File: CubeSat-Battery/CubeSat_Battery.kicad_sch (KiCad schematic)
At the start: 3 parts, among them J1 Conn_01x02_Pin, J2 Conn_01x02_Pin, U1 BatteryPack

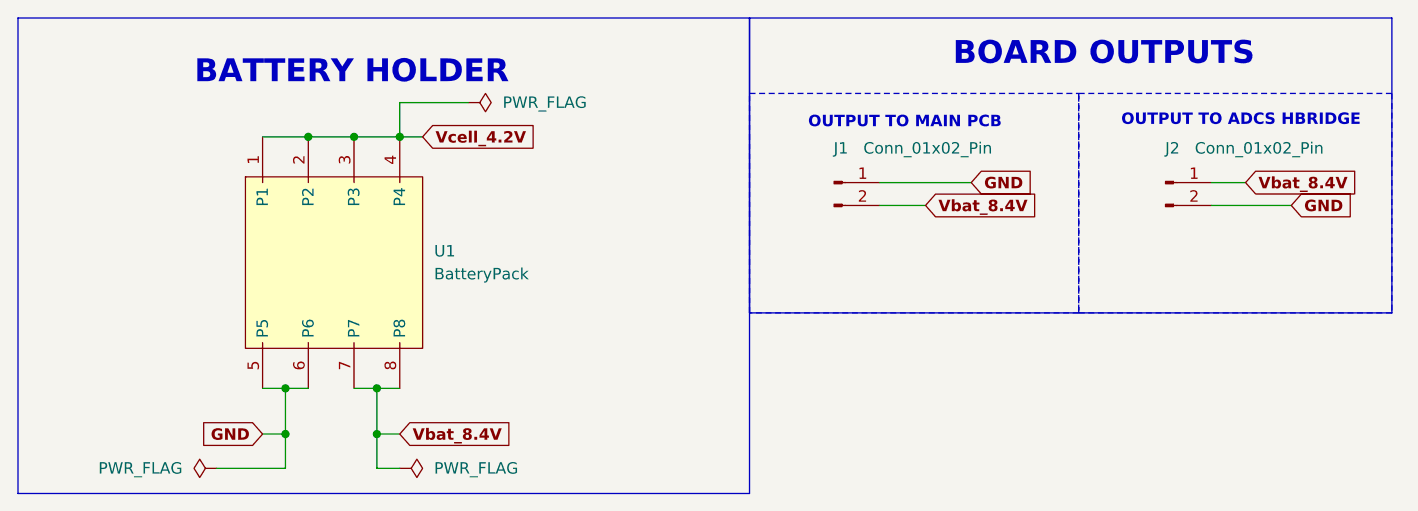
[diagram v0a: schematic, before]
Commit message: final version of the 3 PCBs, minor size changes for the protoypes
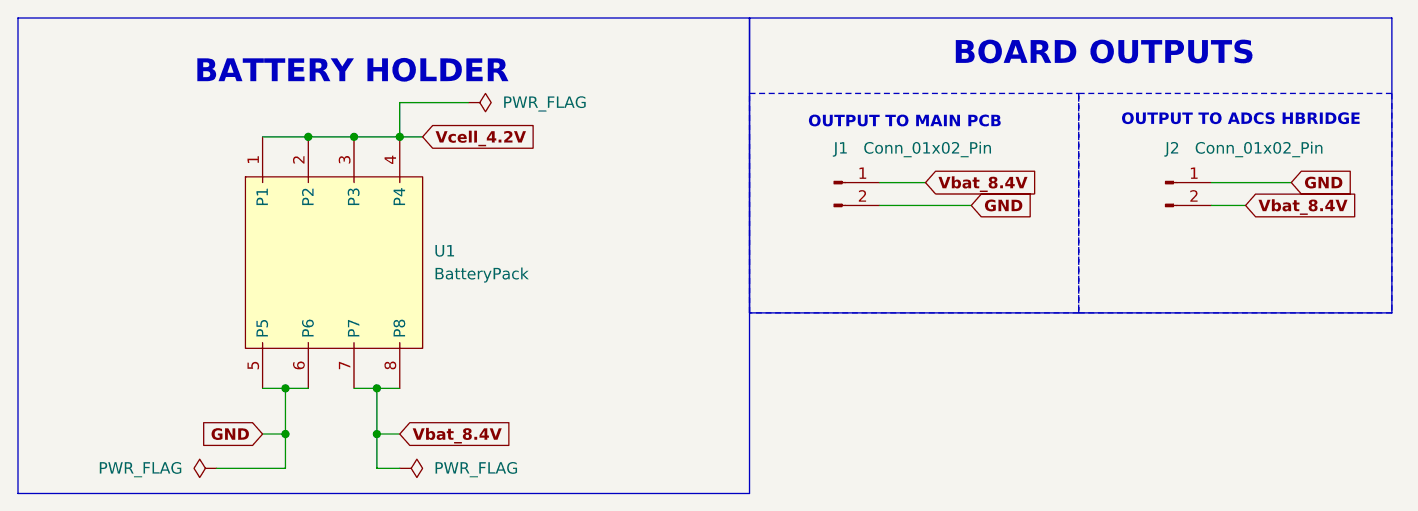
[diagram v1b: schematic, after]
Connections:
- net GND: now also J1.2 (Pin_2), J2.1 (Pin_1); no longer J1.1 (Pin_1), J2.2 (Pin_2)
- net Vbat_8.4V: now also J1.1 (Pin_1), J2.2 (Pin_2); no longer J1.2 (Pin_2), J2.1 (Pin_1)
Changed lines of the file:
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@@
-	(wire
-		(pts
-			(xy 107.95 33.02) (xy 113.03 33.02)
-		)
-		(stroke
-			(width 0)
-			(type default)
-		)
-	)
 	(wire
 		(pts
@@
 	(wire
 		(pts
+			(xy 107.95 30.48) (xy 113.03 30.48)
+		)
+		(stroke
+			(width 0)
+			(type default)
+		)
+	)
+	(wire
+		(pts
 			(xy 41.91 53.34) (xy 44.45 53.34)
 		)
@@
 	(wire
 		(pts
-			(xy 107.95 30.48) (xy 118.11 30.48)
+			(xy 144.78 33.02) (xy 148.59 33.02)
 		)
 		(stroke
@@
 	(wire
 		(pts
-			(xy 144.78 30.48) (xy 148.59 30.48)
-		)
-		(stroke
-			(width 0)
-			(type default)
-		)
-	)
-	(wire
-		(pts
 			(xy 49.53 53.34) (xy 52.07 53.34)
 		)
@@
 	(wire
 		(pts
+			(xy 144.78 30.48) (xy 153.67 30.48)
+		)
+		(stroke
+			(width 0)
+			(type default)
+		)
+	)
+	(wire
+		(pts
 			(xy 52.07 58.42) (xy 52.07 62.23)
 		)
@@
 	(wire
 		(pts
-			(xy 144.78 33.02) (xy 153.67 33.02)
-		)
-		(stroke
-			(width 0)
-			(type default)
-		)
-	)
-	(wire
-		(pts
 			(xy 54.61 25.4) (xy 57.15 25.4)
 		)
@@
 		)
 	)
+	(wire
+		(pts
+			(xy 107.95 33.02) (xy 118.11 33.02)
+		)
+		(stroke
+			(width 0)
+			(type default)
+		)
+	)
 	(global_label "GND"
 		(shape input)
@@
 	(global_label "GND"
 		(shape input)
-		(at 153.67 33.02 0)
-		(fields_autoplaced yes)
-		(effects
-			(font
-				(size 1.27 1.27)
-				(thickness 0.254)
-				(bold yes)
-			)
-			(justify left)
-		)
-		(property "Intersheetrefs" "${INTERSHEET_REFS}"
-			(at 161.0017 33.02 0)
+		(at 153.67 30.48 0)
+		(fields_autoplaced yes)
+		(effects
+			(font
+				(size 1.27 1.27)
+				(thickness 0.254)
+				(bold yes)
+			)
+			(justify left)
+		)
+		(property "Intersheetrefs" "${INTERSHEET_REFS}"
+			(at 161.0017 30.48 0)
 			(effects
 				(font
@@
 	(global_label "GND"
 		(shape input)
-		(at 118.11 30.48 0)
-		(fields_autoplaced yes)
-		(effects
-			(font
-				(size 1.27 1.27)
-				(thickness 0.254)
-				(bold yes)
-			)
-			(justify left)
-		)
-		(property "Intersheetrefs" "${INTERSHEET_REFS}"
-			(at 125.4417 30.48 0)
+		(at 118.11 33.02 0)
+		(fields_autoplaced yes)
+		(effects
+			(font
+				(size 1.27 1.27)
+				(thickness 0.254)
+				(bold yes)
+			)
+			(justify left)
+		)
+		(property "Intersheetrefs" "${INTERSHEET_REFS}"
+			(at 125.4417 33.02 0)
 			(effects
 				(font
@@
 	(global_label "Vbat_8.4V"
 		(shape input)
-		(at 148.59 30.48 0)
-		(fields_autoplaced yes)
-		(effects
-			(font
-				(size 1.27 1.27)
-				(thickness 0.254)
-				(bold yes)
-			)
-			(justify left)
-		)
-		(property "Intersheetrefs" "${INTERSHEET_REFS}"
-			(at 161.2435 30.48 0)
+		(at 148.59 33.02 0)
+		(fields_autoplaced yes)
+		(effects
+			(font
+				(size 1.27 1.27)
+				(thickness 0.254)
+				(bold yes)
+			)
+			(justify left)
+		)
+		(property "Intersheetrefs" "${INTERSHEET_REFS}"
+			(at 161.2435 33.02 0)
 			(effects
 				(font
@@
 	(global_label "Vbat_8.4V"
 		(shape input)
-		(at 113.03 33.02 0)
-		(fields_autoplaced yes)
-		(effects
-			(font
-				(size 1.27 1.27)
-				(thickness 0.254)
-				(bold yes)
-			)
-			(justify left)
-		)
-		(property "Intersheetrefs" "${INTERSHEET_REFS}"
-			(at 125.6835 33.02 0)
-			(effects
-				(font
+		(at 113.03 30.48 0)
+		(fields_autoplaced yes)
+		(effects
+			(font
+				(size 1.27 1.27)
+				(thickness 0.254)
+				(bold yes)
+			)
+			(justify left)
+		)
+		(property "Intersheetrefs" "${INTERSHEET_REFS}"
+			(at 125.6835 30.48 0)
+			(effects
+				(font

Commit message: add new drill format
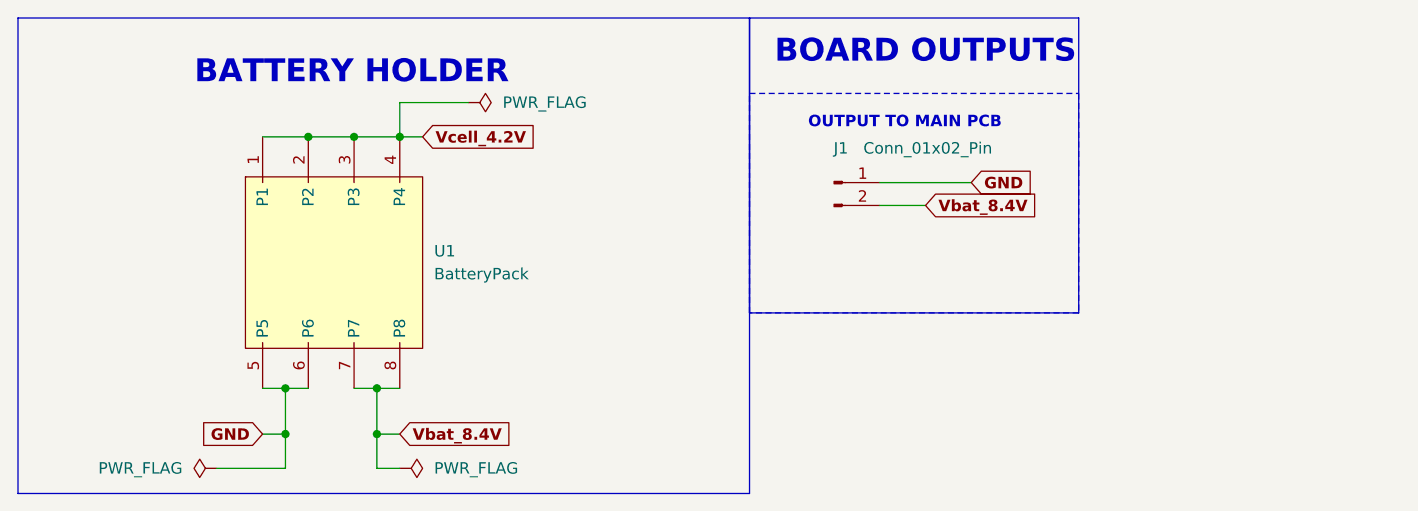
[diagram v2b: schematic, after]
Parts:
- removed J2: Conn_01x02_Pin, Connector_JST:JST_EH_B2B-EH-A_1x02_P2.50mm_Vertical, symbol Connector:Conn_01x02_Pin
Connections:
- net GND: now also J1.1 (Pin_1); no longer J1.2 (Pin_2)
- net Vbat_8.4V: now also J1.2 (Pin_2); no longer J1.1 (Pin_1)
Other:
- note removed: "OUTPUT TO ADCS HBRIDGE"
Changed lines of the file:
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@@
 	(rectangle
 		(start 93.472 12.192)
-		(end 164.846 44.958)
+		(end 130.048 44.958)
 		(stroke
 			(width 0)
@@
 		)
 	)
-	(rectangle
-		(start 130.048 20.574)
-		(end 164.846 44.958)
-		(stroke
-			(width 0)
-			(type dash)
-		)
-		(fill
-			(type none)
-		)
-	)
-	(text "OUTPUT TO ADCS HBRIDGE"
-		(exclude_from_sim no)
-		(at 148.082 23.622 0)
-		(effects
-			(font
-				(size 1.27 1.27)
-				(thickness 0.254)
-				(bold yes)
-			)
-		)
-	)
 	(text "BOARD OUTPUTS"
 		(exclude_from_sim no)
-		(at 132.842 16.256 0)
+		(at 113.03 16.002 0)
 		(effects
 			(font
@@
 	(wire
 		(pts
-			(xy 107.95 30.48) (xy 113.03 30.48)
+			(xy 107.95 33.02) (xy 113.03 33.02)
 		)
 		(stroke
@@
 	(wire
 		(pts
+			(xy 107.95 30.48) (xy 118.11 30.48)
+		)
+		(stroke
+			(width 0)
+			(type default)
+		)
+	)
+	(wire
+		(pts
 			(xy 52.07 53.34) (xy 54.61 53.34)
 		)
@@
 	(wire
 		(pts
-			(xy 144.78 33.02) (xy 148.59 33.02)
-		)
-		(stroke
-			(width 0)
-			(type default)
-		)
-	)
-	(wire
-		(pts
 			(xy 52.07 58.42) (xy 52.07 53.34)
 		)
@@
 	(wire
 		(pts
-			(xy 144.78 30.48) (xy 153.67 30.48)
-		)
-		(stroke
-			(width 0)
-			(type default)
-		)
-	)
-	(wire
-		(pts
 			(xy 52.07 58.42) (xy 52.07 62.23)
 		)
@@
 		(pts
 			(xy 54.61 25.4) (xy 57.15 25.4)
-		)
-		(stroke
-			(width 0)
-			(type default)
-		)
-	)
-	(wire
-		(pts
-			(xy 107.95 33.02) (xy 118.11 33.02)
 		)
 		(stroke
@@
 	(global_label "GND"
 		(shape input)
-		(at 153.67 30.48 0)
+		(at 118.11 30.48 0)
 		(fields_autoplaced yes)
 		(effects
@@
 		)
 		(property "Intersheetrefs" "${INTERSHEET_REFS}"
-			(at 161.0017 30.48 0)
-			(effects
-				(font
-					(size 1.27 1.27)
-				)
-				(justify left)
-				(hide yes)
-			)
-		)
-	)
-	(global_label "GND"
-		(shape input)
-		(at 118.11 33.02 0)
-		(fields_autoplaced yes)
-		(effects
-			(font
-				(size 1.27 1.27)
-				(thickness 0.254)
-				(bold yes)
-			)
-			(justify left)
-		)
-		(property "Intersheetrefs" "${INTERSHEET_REFS}"
-			(at 125.4417 33.02 0)
+			(at 125.4417 30.48 0)
 			(effects
 				(font
@@
 	(global_label "Vbat_8.4V"
 		(shape input)
-		(at 148.59 33.02 0)
+		(at 113.03 33.02 0)
 		(fields_autoplaced yes)
 		(effects
@@
 		)
 		(property "Intersheetrefs" "${INTERSHEET_REFS}"
-			(at 161.2435 33.02 0)
-			(effects
-				(font
-					(size 1.27 1.27)
-				)
-				(justify left)
-				(hide yes)
-			)
-		)
-	)
-	(global_label "Vbat_8.4V"
-		(shape input)
-		(at 113.03 30.48 0)
-		(fields_autoplaced yes)
-		(effects
-			(font
-				(size 1.27 1.27)
-				(thickness 0.254)
-				(bold yes)
-			)
-			(justify left)
-		)
-		(property "Intersheetrefs" "${INTERSHEET_REFS}"
-			(at 125.6835 30.48 0)
+			(at 125.6835 33.02 0)
 			(effects
 				(font
@@
 					(unit 1)
 				)
-			)
-		)
-	)
-	(symbol
-		(lib_id "Connector:Conn_01x02_Pin")
-		(at 139.7 30.48 0)
-		(unit 1)
-		(exclude_from_sim no)
-		(in_bom yes)
-		(on_board yes)
-		(dnp no)
-		(property "Reference" "J2"
-			(at 140.462 26.67 0)
-			(effects
-				(font
-					(size 1.27 1.27)
-				)
-			)
-		)
-		(property "Value" "Conn_01x02_Pin"
-			(at 150.114 26.67 0)
-			(effects
-				(font
-					(size 1.27 1.27)
-				)
-			)
-		)
-		(property "Footprint" "Connector_JST:JST_EH_B2B-EH-A_1x02_P2.50mm_Vertical"
-			(at 139.7 30.48 0)
-			(effects
-				(font
-					(size 1.27 1.27)
-				)
-				(hide yes)
-			)
-		)
-		(property "Datasheet" "~"
-			(at 139.7 30.48 0)
-			(effects
-				(font
-					(size 1.27 1.27)
-				)
-				(hide yes)
-			)
-		)
-		(property "Description" "Generic connector, single row, 01x02, script generated"
-			(at 139.7 30.48 0)
-			(effects
-				(font
-					(size 1.27 1.27)
-				)
-				(hide yes)
-			)
-		)
-		(pin "1"
-		)
-		(pin "2"
-		)
-		(instances
-			(project ""
-				(path "/b0f59bc3-d31e-43eb-8cb8-cd4747043e73"
-					(reference "J2")
-					(unit 1)
-				)

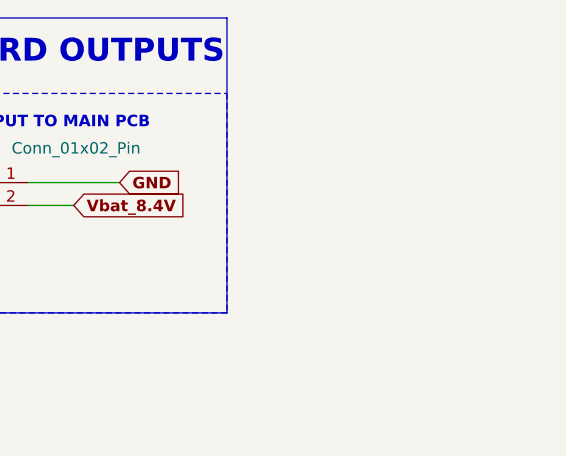
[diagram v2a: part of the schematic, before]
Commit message: final changes in ALL 3 pcbs: mounting wholes config, and a few connector changes
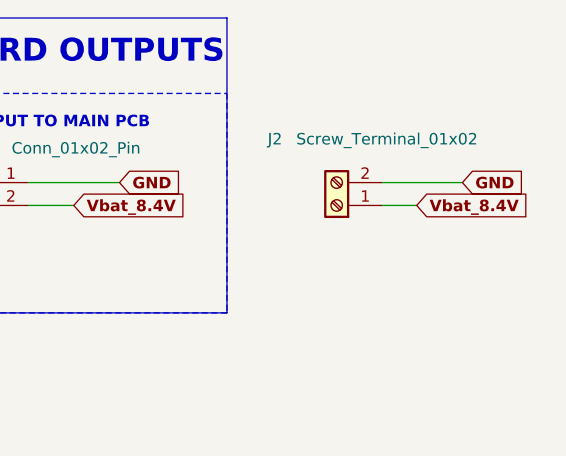
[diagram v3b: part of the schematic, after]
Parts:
- added J2: Screw_Terminal_01x02, TerminalBlock_Phoenix:TerminalBlock_Phoenix_MKDS-1,5-2_1x02_P5.00mm_Horizontal, symbol Connector:Screw_Terminal_01x02
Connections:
- net GND: now also J2.2 (Pin_2)
- net Vbat_8.4V: now also J2.1 (Pin_1)
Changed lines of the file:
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@@
+	(wire
+		(pts
+			(xy 147.32 30.48) (xy 156.21 30.48)
+		)
+		(stroke
+			(width 0)
+			(type default)
+		)
+	)
 	(wire
 		(pts
@@
 	(wire
 		(pts
+			(xy 147.32 33.02) (xy 151.13 33.02)
+		)
+		(stroke
+			(width 0)
+			(type default)
+		)
+	)
+	(wire
+		(pts
 			(xy 107.95 30.48) (xy 118.11 30.48)
 		)
@@
 	(global_label "Vbat_8.4V"
 		(shape input)
+		(at 151.13 33.02 0)
+		(fields_autoplaced yes)
+		(effects
+			(font
+				(size 1.27 1.27)
+				(thickness 0.254)
+				(bold yes)
+			)
+			(justify left)
+		)
+		(property "Intersheetrefs" "${INTERSHEET_REFS}"
+			(at 163.7835 33.02 0)
+			(effects
+				(font
+					(size 1.27 1.27)
+				)
+				(justify left)
+				(hide yes)
+			)
+		)
+	)
+	(global_label "Vbat_8.4V"
+		(shape input)
 		(at 54.61 58.42 0)
 		(fields_autoplaced yes)
@@
 		(property "Intersheetrefs" "${INTERSHEET_REFS}"
 			(at 70.2874 25.4 0)
+			(effects
+				(font
+					(size 1.27 1.27)
+				)
+				(justify left)
+				(hide yes)
+			)
+		)
+	)
+	(global_label "GND"
+		(shape input)
+		(at 156.21 30.48 0)
+		(fields_autoplaced yes)
+		(effects
+			(font
+				(size 1.27 1.27)
+				(thickness 0.254)
+				(bold yes)
+			)
+			(justify left)
+		)
+		(property "Intersheetrefs" "${INTERSHEET_REFS}"
+			(at 163.5417 30.48 0)
 			(effects
 				(font
@@
 					(unit 1)
 				)
+			)
+		)
+	)
+	(symbol
+		(lib_id "Connector:Screw_Terminal_01x02")
+		(at 142.24 33.02 180)
+		(unit 1)
+		(exclude_from_sim no)
+		(in_bom yes)
+		(on_board yes)
+		(dnp no)
+		(property "Reference" "J2"
+			(at 135.382 25.654 0)
+			(effects
+				(font
+					(size 1.27 1.27)
+				)
+			)
+		)
+		(property "Value" "Screw_Terminal_01x02"
+			(at 147.828 25.654 0)
+			(effects
+				(font
+					(size 1.27 1.27)
+				)
+			)
+		)
+		(property "Footprint" "TerminalBlock_Phoenix:TerminalBlock_Phoenix_MKDS-1,5-2_1x02_P5.00mm_Horizontal"
+			(at 142.24 33.02 0)
+			(effects
+				(font
+					(size 1.27 1.27)
+				)
+				(hide yes)
+			)
+		)
+		(property "Datasheet" "~"
+			(at 142.24 33.02 0)
+			(effects
+				(font
+					(size 1.27 1.27)
+				)
+				(hide yes)
+			)
+		)
+		(property "Description" "Generic screw terminal, single row, 01x02, script generated (kicad-library-utils/schlib/autogen/connector/)"
+			(at 142.24 33.02 0)
+			(effects
+				(font
+					(size 1.27 1.27)
+				)
+				(hide yes)
+			)
+		)
+		(pin "1"
+		)
+		(pin "2"
+		)
+		(instances
+			(project "CubeSat_Battery"
+				(path "/b0f59bc3-d31e-43eb-8cb8-cd4747043e73"
+					(reference "J2")
+					(unit 1)
+				)
